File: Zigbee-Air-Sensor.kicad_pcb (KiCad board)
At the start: 4 copper layers, 34 x 45 mm, 79 parts, among them J1 USB_C_Receptacle_PowerOnly_6P, J2 Conn_01x04, J3 FH34SRJ-6S-0.5SH, J4 FH34SRJ-6S-0.5SH, J5 Conn_01x06, J6 E-Ink 24P, Q1 BC847W, Q2 CJ2101, Q3 Si1308EDL, U1 ESP32-H2-MINI-1-H4, U2 BQ25628ERYKR, U3 BQ27426YZFR, U4 TPS63030DSK, U5 SHT30-DIS, U6 LPS22DF

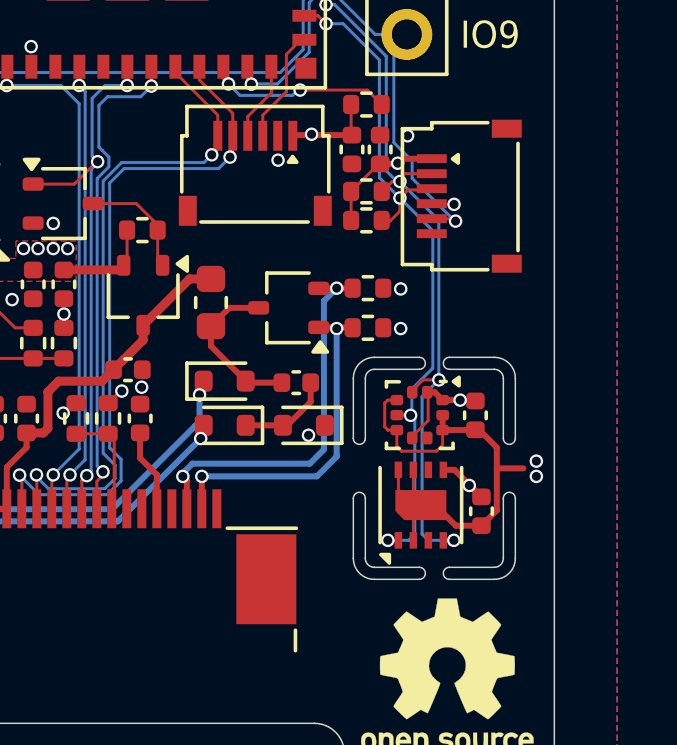
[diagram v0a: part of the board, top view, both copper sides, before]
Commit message: fixed: line to edge clearance
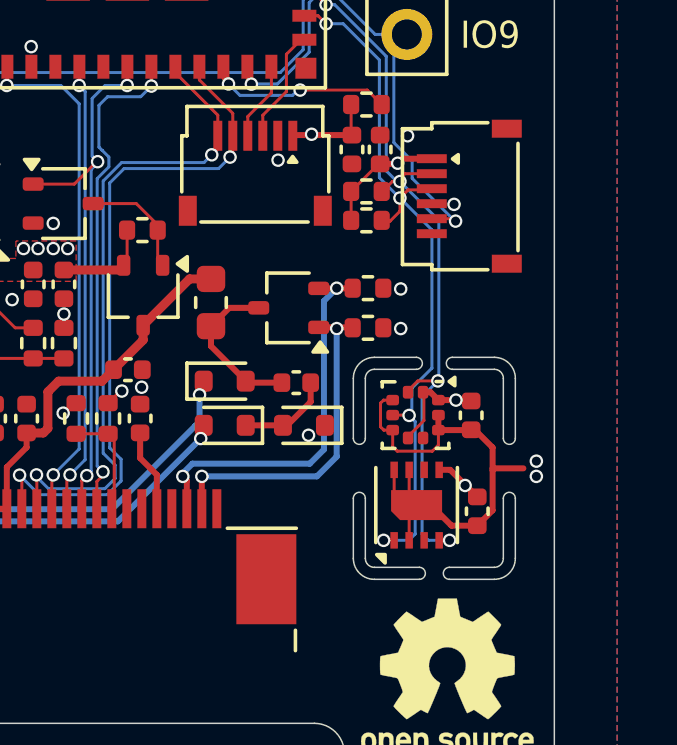
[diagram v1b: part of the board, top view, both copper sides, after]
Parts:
- moved U5 0.14 mm to (129.4, 130.7)
- moved U6 0.14 mm to (129.4, 127.7)
- moved C32 0.14 mm to (131.4, 130.9)
- moved C33 0.14 mm to (131.2, 127.7)
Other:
- outline, holes or cut-outs redrawn

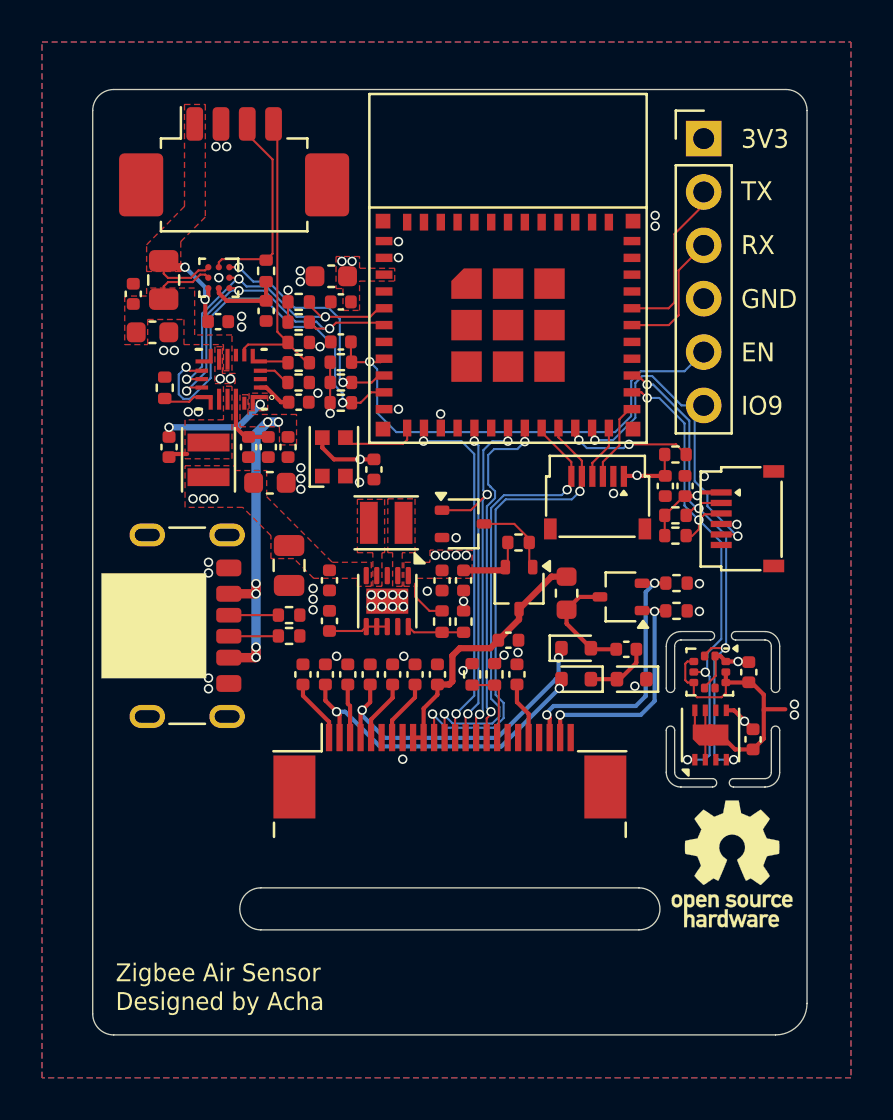
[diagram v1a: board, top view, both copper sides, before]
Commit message: slots width & pos oshw logo layer component re-location add mounting hole
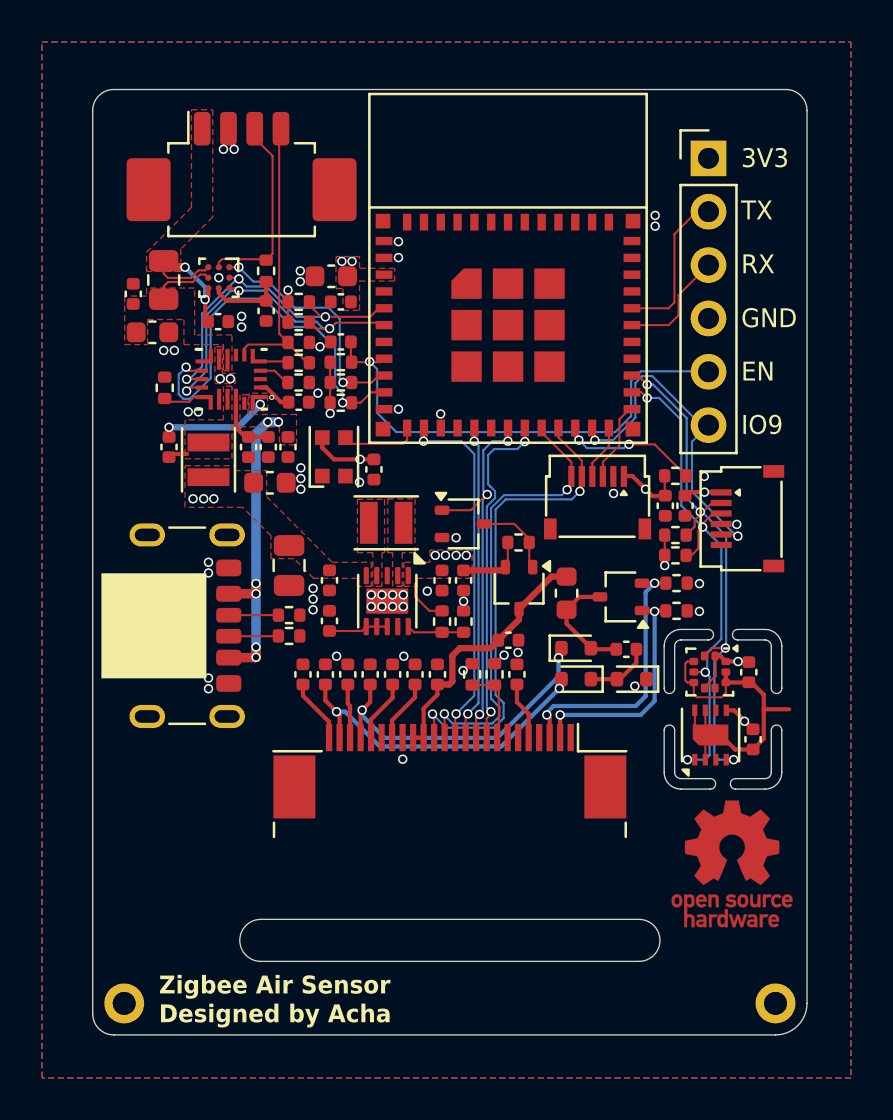
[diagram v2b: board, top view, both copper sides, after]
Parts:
- added REF**: MountingHole_1.1mm_M1_Pad, Zigbee-Air-Sensor:MountingHole_1.1mm_M1_Pad, F.Cu at (101.5, 143.5)
- added REF**: MountingHole_1.1mm_M1_Pad, Zigbee-Air-Sensor:MountingHole_1.1mm_M1_Pad, F.Cu at (132.5, 143.5)
- added REF**: OSHW-Logo_5.7x6mm_Copper, Zigbee-Air-Sensor:OSHW-Logo_5.7x6mm_Copper, F.Cu at (130.4, 136.9)
- #SYM1: value OSHW-Logo_5.7x6mm_SilkScreen -> OSHW-Logo_5.7x6mm_Mask; footprint Symbol:OSHW-Logo_5.7x6mm_SilkScreen -> Zigbee-Air-Sensor:OSHW-Logo_5.7x6mm_Mask
- moved R8 1.02 mm to (127.7, 118.4)
- moved J5 0.97 mm to (129.3, 103.3)
- moved C2 0.94 mm to (127.3, 119.8)
- moved C3 0.94 mm to (128.2, 119.8), turned to -90 degrees
- moved R5 0.94 mm to (127.7, 122.2)
- moved R6 0.94 mm to (127.7, 121.2)
- moved J2 0.42 mm to (107.1, 104.3)
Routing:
- net /ESP32-H2/ESP32_RXD0: track 6.24 -> 5.39 mm
- net /Sensors/SDA: track 24.5 -> 25.1 mm
- net /Sensors/SCL: track 25.0 -> 25.6 mm
- net /ESP32-H2/ESP32_TXD0: track 7.97 -> 7.45 mm
- net +3V3: track 30.3 -> 30.0 mm, vias 14 -> 15
- net GND: track 15.7 -> 15.8 mm, vias 54 -> 52
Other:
- outline, holes or cut-outs redrawn

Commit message: Add R24 Add testpoint for I2C Change CI image tag
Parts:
- added R24: 10K, Resistor_SMD:R_0402_1005Metric, F.Cu at (117.8, 118.8)
- added TP1: TestPoint, Zigbee-Air-Sensor:TestPoint_Pad_D0.6mm, F.Cu at (102.4, 114.2)
- added TP2: TestPoint, Zigbee-Air-Sensor:TestPoint_Pad_D0.6mm, F.Cu at (102.4, 113.1)
- added TP3: TestPoint, Zigbee-Air-Sensor:TestPoint_Pad_D0.6mm, F.Cu at (130.4, 123.6)
- added TP4: TestPoint, Zigbee-Air-Sensor:TestPoint_Pad_D0.6mm, F.Cu at (131.5, 123.6)
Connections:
- Q1 pad 1: /E-Ink/RES -> Net-(Q1-B)
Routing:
- net /Sensors/SCL: track 25.6 -> 30.7 mm
- net /Sensors/SDA: track 25.1 -> 30.1 mm
- net /BQ25628E/SDA: track 15.7 -> 18.3 mm
- net /BQ25628E/SCL: track 16.1 -> 18.2 mm
- net /E-Ink/RES: track 18.4 -> 16.6 mm
- net Net-(Q1-B): track 0.00 -> 1.48 mm
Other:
- board text added: "PTH"
